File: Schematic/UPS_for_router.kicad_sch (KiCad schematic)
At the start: 21 parts, among them J1 12V-IN, J2 12V-IN, J3 BAT IN, J4 12V-OUT, J5 9V-OUT, J6 12V out, K1 FINDER-36.11, SW1 SW_SPST, U1 L7809

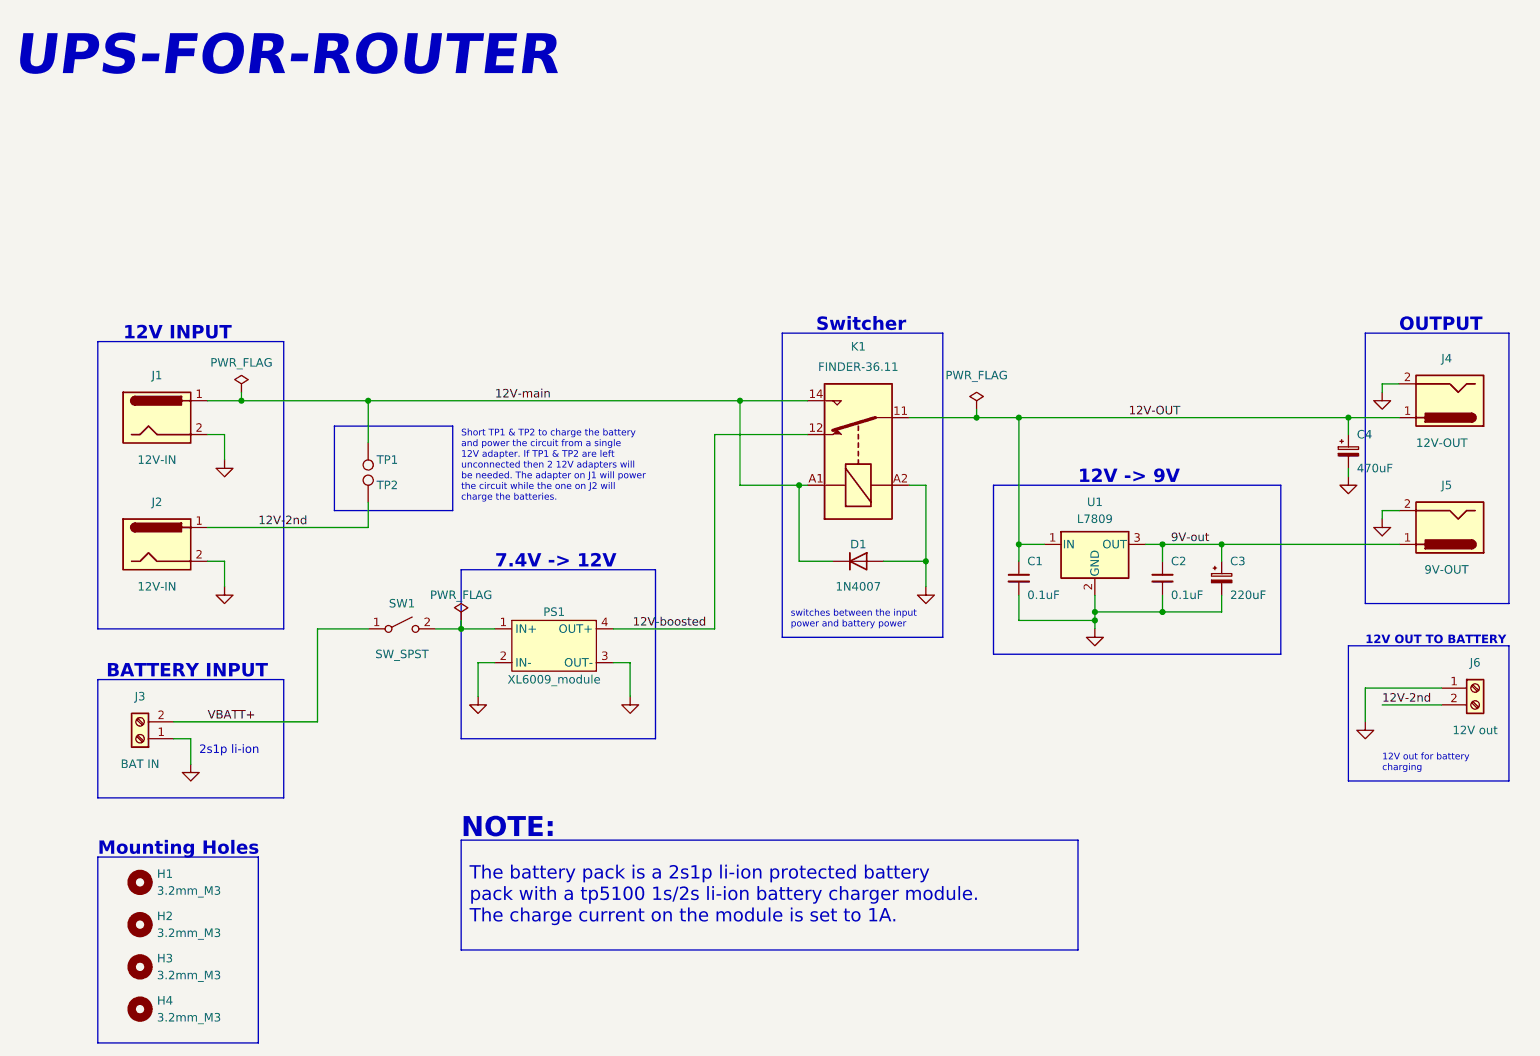
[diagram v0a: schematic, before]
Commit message: updated schematic and PCB
removed relay and added diode as well as updated the PCB
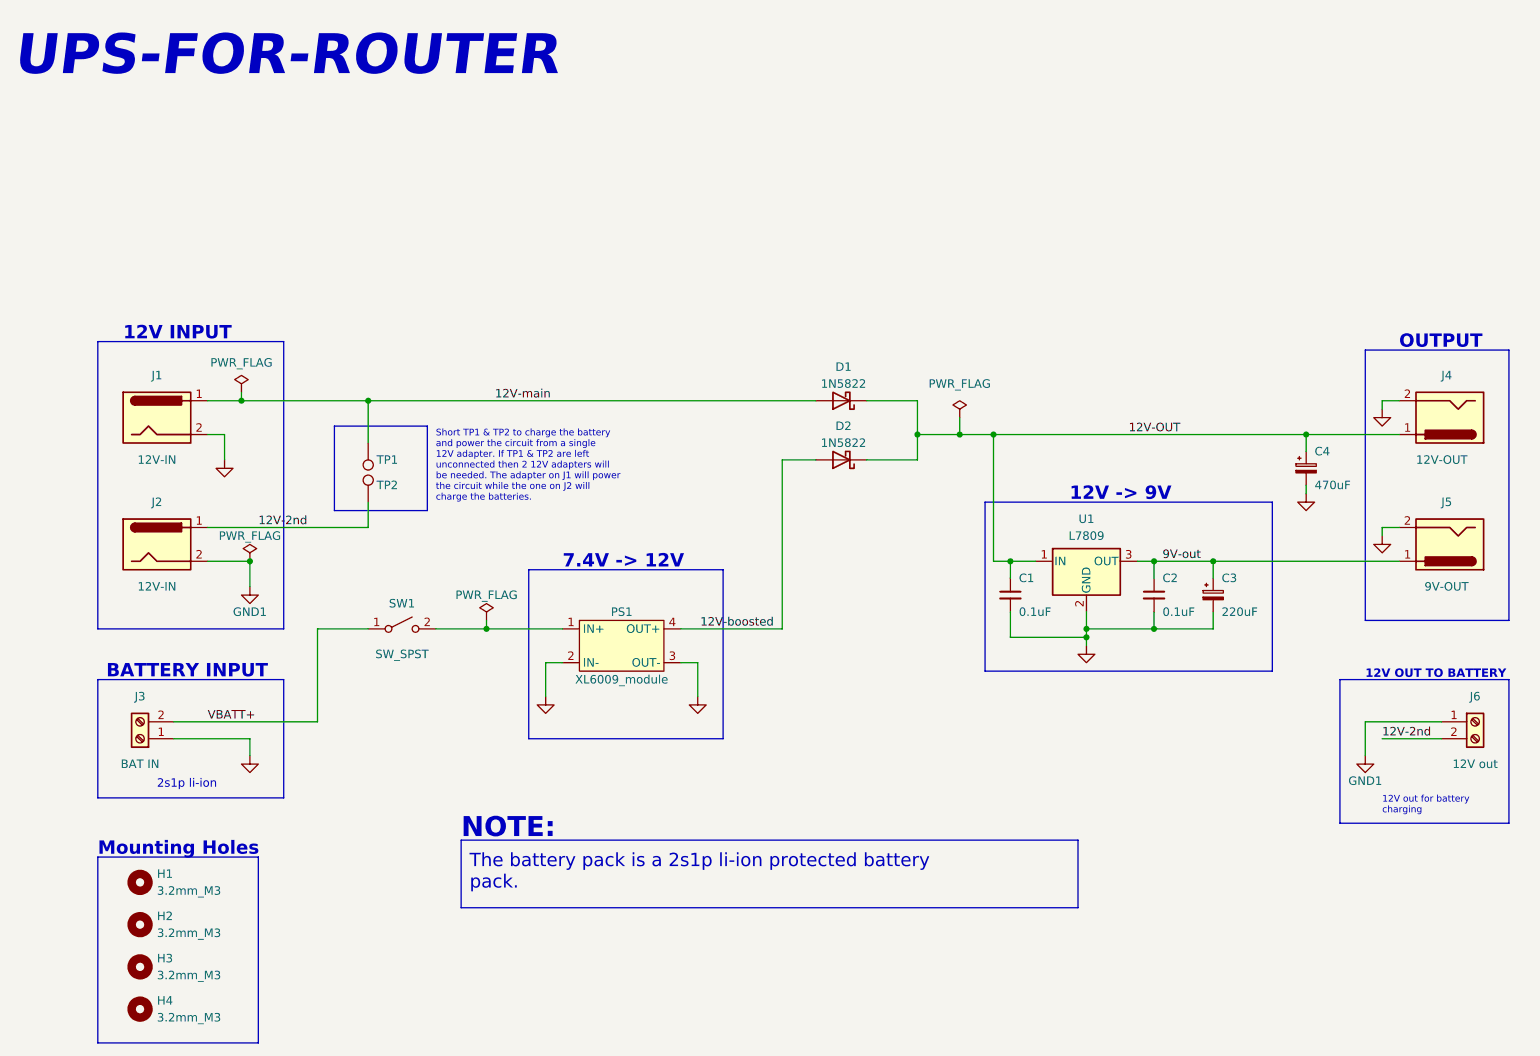
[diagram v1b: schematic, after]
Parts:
- removed D1: 1N4007, Diode_THT:D_DO-41_SOD81_P10.16mm_Horizontal, symbol Diode:1N4007
- removed K1: FINDER-36.11, Relay_THT:Relay_SPDT_Finder_36.11, symbol Relay:FINDER-36.11
- added D1, D2: 1N5822, Diode_THT:D_DO-201AD_P15.24mm_Horizontal, symbol Diode:1N5822
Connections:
- net 12V-OUT: now also D1.1 (K), D2.1 (K)
- net 12V-boosted: now also D2.2 (A)
- net 12V-main: now also D1.2 (A)
- net GND: no longer J2.2, J6.1 (Pin_1)
- new net GND1: J2.2, J6.1 (Pin_1)
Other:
- note added: "The battery pack is a 2s1p li-ion protected battery pack."
- note removed: "Switcher"
- note removed: "The battery pack is a 2s1p li-ion protected battery pack with a tp5100 1s/2s li-ion battery charger module. The charge current on the module is set to 1A."
- note removed: "switches between the input power and battery power"
- moved on the sheet: C1, C2, C3, C4, J4, J5, J6, PS1, U1
